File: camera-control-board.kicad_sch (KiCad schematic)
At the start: 24 parts, among them J1 DF12NB-36DS-0.5V_51_, J2 10104110-0001LF, J3 104031-0811, U1 STM32H743IITx, U2 IS42S32800J-7TLI, Y2 Crystal_GND2

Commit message: configured library and repo correctly. edits incoming
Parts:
- J1: symbol DF12NB-36DS-0.5V_51_:DF12NB-36DS-0.5V_51_ -> Argus_Connectors:DF12NB-36DS-0.5V_51_
- J2: symbol 10104110-0001LF:10104110-0001LF -> Argus_Connectors:10104110-0001LF
- J3: symbol 104031-0811:104031-0811 -> Argus_Connectors:104031-0811
- L1: symbol 2024-09-28_22-13-49:MPZ1608S181ATAH0 -> Argus_Misc:MPZ1608S181ATAH0
- RN1: symbol EXB-V8V103JV:EXB-V8V103JV -> Argus_Misc:EXB-V8V103JV
- U2: symbol IS42S32800J-7TLI:IS42S32800J-7TLI -> Argus_ICs:IS42S32800J-7TLI
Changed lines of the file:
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@@
 	)
 	(symbol
-		(lib_id "DF12NB-36DS-0.5V_51_:DF12NB-36DS-0.5V_51_")
+		(lib_id "Argus_Connectors:DF12NB-36DS-0.5V_51_")
 		(at 405.13 88.9 0)
 		(unit 1)
@@
 	)
 	(symbol
-		(lib_id "IS42S32800J-7TLI:IS42S32800J-7TLI")
+		(lib_id "Argus_ICs:IS42S32800J-7TLI")
 		(at 307.34 125.73 0)
 		(unit 1)
@@
 	)
 	(symbol
-		(lib_id "104031-0811:104031-0811")
+		(lib_id "Argus_Connectors:104031-0811")
 		(at 524.51 45.72 0)
 		(unit 1)
@@
 	)
 	(symbol
-		(lib_id "2024-09-28_22-13-49:MPZ1608S181ATAH0")
+		(lib_id "Argus_Misc:MPZ1608S181ATAH0")
 		(at 231.14 38.1 90)
 		(unit 1)
@@
 	)
 	(symbol
-		(lib_id "EXB-V8V103JV:EXB-V8V103JV")
+		(lib_id "Argus_Misc:EXB-V8V103JV")
 		(at 513.08 91.44 0)
 		(unit 1)
@@
 	)
 	(symbol
-		(lib_id "10104110-0001LF:10104110-0001LF")
+		(lib_id "Argus_Connectors:10104110-0001LF")
 		(at 107.95 322.58 0)
 		(unit 1)

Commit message: adding LDOs, changed schematic sheet size
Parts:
- added U3: XC6210B332MR-G, SOT-25_TOR, symbol Argus_ICs:XC6210B332MR-G
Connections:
- net VCC: no longer C1.1, C9.1, J1.2, J1.20, J1.30, J1.36, J3.4 (VDD), L1.1, R2.1, R3.1, R4.2, R7.1, RN1.1, RN1.2, RN1.3, RN1.4, U1.103 (VDD), U1.114 (VDD33_USB), U1.127 (VDD), U1.136 (VDD), U1.149 (VDD), U1.15 (VDD), U1.159 (VDD), U1.171 (PDR_ON), U1.172 (VDD), U1.23 (VDD), U1.36 (VDD), U1.49 (VDD), U1.6 (VBAT), U1.62 (VDD), U1.72 (VDD), U1.82 (VDD), U1.91 (VDD), U2.1 (VDD_2), U2.15 (VDD_3), U2.29 (VDD_4), U2.3 (VDDQ_2), U2.35 (VDDQ_5), U2.41 (VDDQ_8), U2.43 (VDD), U2.49 (VDDQ_3), U2.55 (VDDQ), U2.75 (VDDQ_4), U2.81 (VDDQ_6), U2.9 (VDDQ_7)
- new net +3.3V: C1.1, C9.1, J1.2, J1.20, J1.30, J1.36, J3.4 (VDD), L1.1, R2.1, R3.1, R4.2, R7.1, RN1.1, RN1.2, RN1.3, RN1.4, U1.103 (VDD), U1.114 (VDD33_USB), U1.127 (VDD), U1.136 (VDD), U1.149 (VDD), U1.15 (VDD), U1.159 (VDD), U1.171 (PDR_ON), U1.172 (VDD), U1.23 (VDD), U1.36 (VDD), U1.49 (VDD), U1.6 (VBAT), U1.62 (VDD), U1.72 (VDD), U1.82 (VDD), U1.91 (VDD), U2.1 (VDD_2), U2.15 (VDD_3), U2.29 (VDD_4), U2.3 (VDDQ_2), U2.35 (VDDQ_5), U2.41 (VDDQ_8), U2.43 (VDD), U2.49 (VDDQ_3), U2.55 (VDDQ), U2.75 (VDDQ_4), U2.81 (VDDQ_6), U2.9 (VDDQ_7)
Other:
- note added: "LDOs (Voltage Regulation)"
- note added: "MCU (STM32H743IITx)"
- moved on the sheet: C2, C3, C4, C5, C6, C7, C8, L1, R4, R5, R6, U1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

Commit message: Most of revisions finished. Added Flash.
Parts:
- removed C1: 47u, symbol Device:C_Polarized_US
- removed C2, C3: 12p, symbol Device:C
- removed C4: 1u, symbol Device:C
- removed C9: .1u, symbol Device:C
- removed R4: 10K, symbol Device:R
- removed RN1: EXB-V8V103JV, EXB38V472JV, symbol Argus_Misc:EXB-V8V103JV
- removed U3: XC6210B332MR-G, SOT-25_TOR, symbol Argus_ICs:XC6210B332MR-G
- removed Y2: Crystal_GND2, symbol Device:Crystal_GND2
- added C10, C19: 1uF, Capacitor_SMD:C_0603_1608Metric, symbol Device:C_Small
- added C11, C12: 4pF, Capacitor_SMD:C_0603_1608Metric, symbol Device:C_Small
- added C13, C14, C15, C16, C17, C3, C4: 0.1uF, Capacitor_SMD:C_0603_1608Metric, symbol Device:C_Small
- added C18: 47uF, Capacitor_SMD:C_0201_0603Metric, symbol Device:C_Polarized_Small_US
- added C2: 47uF, Capacitor_SMD:C_0603_1608Metric, symbol Device:C_Polarized_Small_US
- added D2: LED_RGBA, LED_SMD:LED_RGB_Wuerth-PLCC4_3.2x2.8mm_150141M173100, symbol Device:LED_RGBA
- added J4: 02x05 M 1.27mm, Connector_PinHeader_1.27mm:PinHeader_2x05_P1.27mm_Vertical_SMD, symbol Connector_Generic:Conn_02x05_Odd_Even
- added J5: Conn_01x08, Connector_PinHeader_2.54mm:PinHeader_1x08_P2.54mm_Vertical, symbol Connector_Generic:Conn_01x08
- added R10: 560, Resistor_SMD:R_0603_1608Metric, symbol Device:R
- added R11: 1K, Resistor_SMD:R_0603_1608Metric, symbol Device:R_Small
- added R16, R17, R18, R19, R20, R21, R8, R9: 10K, Resistor_SMD:R_0603_1608Metric, symbol Device:R_Small
- added R4: 100R, Resistor_SMD:R_0603_1608Metric, symbol Device:R_Small
- added RN2: 330R, Resistor_SMD:R_Array_Concave_4x0603, symbol Device:R_Pack04
- added SW1: CAS-120TA, cameraboard:CAS-120TA, symbol Switch:SW_SPDT
- added SW2: KMR2x, mainboard:BTN_KMR2, symbol Switch:SW_Push
- added U3: W25Q256JVEIQ TR, Argus_ICs:WSON8_E_WIN-L, symbol Argus_ICs:W25Q256JVEIQ_TR
- added U4: XC6210B332MR, Package_TO_SOT_SMD:SOT-23-5, symbol Regulator_Linear:XC6210B332MR
- added Y1: 12MHz/7pF, Crystal:Crystal_SMD_2520-4Pin_2.5x2.0mm, symbol Device:Crystal_GND24_Small
- C5, C6, C7, C8: footprint (none) -> Capacitor_SMD:C_0603_1608Metric
- J1: footprint DF12NB-36DS-0.5V_51_:HRS_DF12NB-36DS-0.5V_51_ -> Argus_Connectors:HRS_DF12NB-36DS-0.5V_51_
- J2: footprint 10104110-0001LF:AMPHENOL_10104110-0001LF -> Argus_Connectors:AMPHENOL_10104110-0001LF
- J3: footprint 104031-0811:MOLEX_104031-0811 -> Connector_Card:microSD_HC_Molex_104031-0811; symbol Argus_Connectors:104031-0811 -> Argus_Connectors:USD-1040310811
- R1, R2, R3, R5, R6: footprint (none) -> Resistor_SMD:R_0603_1608Metric
- R7: value R -> 10k
- U2: footprint IS42S32800J-7TLI:SOP50P1176X120-86N -> Argus_ICs:SOP50P1176X120-86N
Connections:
- net DRAM_CKE is gone; now on net DRAM_CLKE: U2.67 (CKE)
- net +3.3V: now also J1.10, C10.1, C13.2, C14.2, C15.2, C16.2, C17.2, C18.1, C19.2, C2.1, C3.2, D2.4 (A), J4.1 (Pin_1), J5.7 (Pin_7), R10.2, R11.1, R16.1, R17.1, R18.1, R19.1, R20.1, R21.1, R8.1, SW1.1 (A), U3.8 (VCC), U4.5 (VOUT)
- net BOOT0: now also R9.2
- net DRAM_D31: no longer U1.12 (PI10)
- net GND: now also J3.11 (SHD), C10.2, C11.1, C12.2, C13.1, C14.1, C15.1, C16.1, C17.1, C18.2, C19.1, C2.2, C3.1, C4.2, J4.3 (Pin_3), J4.5 (Pin_5), J5.8 (Pin_8), R4.2, RN2.4 (R4.1), RN2.5 (R4.2), SW1.3 (C), U3.4 (GND), U3.9 (EPAD), U4.2 (GND), Y1.2, Y1.4; no longer J3.10 (SW-2), J3.G1 (GND), J3.G2 (GND__1), J3.G3 (GND__2), J3.G4 (GND__3)
- net I2C1_SCL: now also J1.32, R2.2
- net I2C1_SDA: now also J1.34, R3.2
- net I2C2_SCL: now also J5.6 (Pin_6)
- net I2C2_SDA: now also J5.5 (Pin_5)
- net LED_B: now also RN2.3 (R3.1)
- net LED_G: now also RN2.2 (R2.1)
- net LED_R: now also RN2.1 (R1.1)
- net OSC_IN: now also C11.2, Y1.3
- net OSC_OUT: now also C12.1, Y1.1
- net SDIO_CMD: now also R17.2; no longer R7.2
- net SDIO_D0: now also J3.7 (DAT0), R18.2
- net SDIO_D1: now also J3.8 (DAT1), R19.2
- net SDIO_D2: now also J3.1 (DAT2), R20.2
- net SDIO_D3: now also J3.2 (DAT3/CD), R21.2
- net SD_CD: now also J3.10 (CD), R16.2
- net SPI2_MISO: now also J5.2 (Pin_2)
- net SPI2_MOSI: now also J5.1 (Pin_1)
- net SPI2_NSS: now also J5.4 (Pin_4)
- net SPI2_SCLK: now also J5.3 (Pin_3)
- net SWCLK: now also J4.4 (Pin_4), R11.2
- net SWDIO: now also J4.2 (Pin_2)
- net VBUS_R: now also R10.1
- net VCC: now also U4.1 (VIN), U4.3 (CE)
- net NRST: now reaches U1.31 (NRST)
- net NRST: now also C4.1, J4.10 (Pin_10), R8.2, SW2.2
- net FLASH_CS: now reaches U1.110 (PG6)
- net FLASH_CS: now also R7.2, U3.1 (/CS)
- net FLASH_IO3: now reaches U1.24 (PF6)
- net FLASH_IO3: now also U3.7 (/HOLD_OR_/RESET(IO3))
- net FLASH_IO2: now reaches U1.25 (PF7)
- net FLASH_IO2: now also U3.3 (/WP(IO2))
- net FLASH_IO0: now reaches U1.26 (PF8)
- net FLASH_IO0: now also U3.5 (DI(IO0))
- net FLASH_IO1: now reaches U1.27 (PF9)
- net FLASH_IO1: now also U3.2 (DO(IO1))
- net FLASH_CLK: now reaches U1.28 (PF10)
- net FLASH_CLK: now also U3.6 (CLK)
- new net: D2.1 (RK), RN2.8 (R1.2)
- new net: D2.2 (GK), RN2.7 (R2.2)
- new net: D2.3 (BK), RN2.6 (R3.2)
- new net: R4.1, SW2.1
- new net: R9.1, SW1.2 (B)
- no-connect marks 0 -> 4
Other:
- note added: "(Not Populated)"
- note added: "Decoupling Caps"
- note added: "Reset & Boot0 Switches"
- note added: "SWD Connector"
- note added: "Select boot mode Set "low" for normal operation. Set "high" for bootloader mode"
- note added: "Set for flight"
- note added: "Status LEDs, IO Headers"
- note added: "Status RGB LED"
- moved on the sheet: C5, C6, L1, R1, U2

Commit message: Schematic Revs Finished.
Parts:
- added C1: 1uF, Capacitor_SMD:C_0603_1608Metric, symbol Device:C_Small
- added VR1: AP7366-28W5-7, AP7366-28W5-7:SOT95P285X140-5N, symbol Argus_ICs:AP7366-28W5-7
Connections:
- net DCMI_FSIN: now also J4.6 (Pin_6)
- net GND: now also C1.2, VR1.2 (GND)
- net VCC: now also VR1.1 (IN), VR1.3 (EN)
- net VDDA: now also C1.1, VR1.5 (OUT)
- no-connect marks 4 -> 3
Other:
- note added: "Flash Memory"
- note added: "SD Card Connector"
- note removed: "(Not Populated)"
- moved on the sheet: C10, C11, C12, C13, C14, C15, C16, C17, C18, C19, C2, C3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

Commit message: all footprints accounted for.
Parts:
- removed SW2: KMR2x, mainboard:BTN_KMR2, symbol Switch:SW_Push
- added SW3: SW_Push, Argus_Misc:BTN_KMR2, symbol Switch:SW_Push
- L1: footprint IND_1608_TDK -> Argus_Misc:IND_1608_TDK
- R7: footprint (none) -> Resistor_SMD:R_0603_1608Metric
- SW1: footprint cameraboard:CAS-120TA -> Argus_Misc:CAS-120TA
- VR1: footprint AP7366-28W5-7:SOT95P285X140-5N -> Argus_ICs:SOT95P285X140-5N
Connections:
- net NRST: now also SW3.2
- net at R4.1: now also SW3.1
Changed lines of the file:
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@@
 	)
 	(symbol
-		(lib_id "Switch:SW_Push")
-		(at 179.07 72.39 0)
-		(unit 1)
-		(exclude_from_sim no)
-		(in_bom yes)
-		(on_board yes)
-		(dnp no)
-		(property "Reference" "SW2"
-			(at 179.07 65.786 0)
-			(effects
-				(font
-					(size 1.27 1.27)
-				)
-			)
-		)
-		(property "Value" "KMR2x"
-			(at 179.07 68.0974 0)
-			(effects
-				(font
-					(size 1.27 1.27)
-				)
-			)
-		)
-		(property "Footprint" "mainboard:BTN_KMR2"
-			(at 179.07 67.31 0)
-			(effects
-				(font
-					(size 1.27 1.27)
-				)
-				(hide yes)
-			)
-		)
-		(property "Datasheet" "~"
-			(at 179.07 67.31 0)
-			(effects
-				(font
-					(size 1.27 1.27)
-				)
-				(hide yes)
-			)
-		)
-		(property "Description" ""
-			(at 179.07 72.39 0)
-			(effects
-				(font
-					(size 1.27 1.27)
-				)
-				(hide yes)
-			)
-		)
-		(pin "1"
-		)
-		(pin "2"
-		)
-		(instances
-			(project "camera-control-board"
-				(path "/a6ed6f18-4f86-494f-813d-c58250854c51"
-					(reference "SW2")
-					(unit 1)
-				)
-			)
-		)
-	)
-	(symbol
 		(lib_id "power:VCC")
 		(at 156.21 27.94 0)
@@
 			)
 		)
-		(property "Footprint" "cameraboard:CAS-120TA"
+		(property "Footprint" "Argus_Misc:CAS-120TA"
 			(at 217.932 71.12 0)
 			(effects
@@
 			)
 		)
-		(property "Footprint" ""
+		(property "Footprint" "Resistor_SMD:R_0603_1608Metric"
 			(at 278.892 204.47 90)
 			(effects
@@
 			)
 		)
-		(property "Footprint" "IND_1608_TDK"
+		(property "Footprint" "Argus_Misc:IND_1608_TDK"
 			(at 123.19 34.29 0)
 			(effects
@@
 	)
 	(symbol
+		(lib_id "Switch:SW_Push")
+		(at 179.07 72.39 0)
+		(unit 1)
+		(exclude_from_sim no)
+		(in_bom yes)
+		(on_board yes)
+		(dnp no)
+		(fields_autoplaced yes)
+		(property "Reference" "SW3"
+			(at 179.07 64.77 0)
+			(effects
+				(font
+					(size 1.27 1.27)
+				)
+			)
+		)
+		(property "Value" "SW_Push"
+			(at 179.07 67.31 0)
+			(effects
+				(font
+					(size 1.27 1.27)
+				)
+			)
+		)
+		(property "Footprint" "Argus_Misc:BTN_KMR2"
+			(at 179.07 67.31 0)
+			(effects
+				(font
+					(size 1.27 1.27)
+				)
+				(hide yes)
+			)
+		)
+		(property "Datasheet" "~"
+			(at 179.07 67.31 0)
+			(effects
+				(font
+					(size 1.27 1.27)
+				)
+				(hide yes)
+			)
+		)
+		(property "Description" "Push button switch, generic, two pins"
+			(at 179.07 72.39 0)
+			(effects
+				(font
+					(size 1.27 1.27)
+				)
+				(hide yes)
+			)
+		)
+		(pin "1"
+		)
+		(pin "2"
+		)
+		(instances
+			(project ""
+				(path "/a6ed6f18-4f86-494f-813d-c58250854c51"
+					(reference "SW3")
+					(unit 1)
+				)
+			)
+		)
+	)
+	(symbol
 		(lib_id "power:GND")
 		(at 252.73 36.957 0)
@@
 			)
 		)
-		(property "Footprint" "AP7366-28W5-7:SOT95P285X140-5N"
+		(property "Footprint" "Argus_ICs:SOT95P285X140-5N"
 			(at 233.68 31.75 0)
 			(effects

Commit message: Layout begun.
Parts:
- J5: value Conn_01x08 -> Conn_01x09; footprint Connector_PinHeader_2.54mm:PinHeader_1x08_P2.54mm_Vertical -> Connector_PinHeader_2.54mm:PinHeader_1x09_P2.54mm_Vertical; symbol Connector_Generic:Conn_01x08 -> Connector_Generic:Conn_01x09
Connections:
- net +3.3V: now also J5.8 (Pin_8); no longer J5.7 (Pin_7)
- net DCMI_FSIN: now also J5.1 (Pin_1); no longer J4.6 (Pin_6)
- net GND: now also J5.9 (Pin_9); no longer J5.8 (Pin_8)
- net I2C2_SCL: now also J5.7 (Pin_7); no longer J5.6 (Pin_6)
- net I2C2_SDA: now also J5.6 (Pin_6); no longer J5.5 (Pin_5)
- net SPI2_MISO: now also J5.3 (Pin_3); no longer J5.2 (Pin_2)
- net SPI2_MOSI: now also J5.2 (Pin_2); no longer J5.1 (Pin_1)
- net SPI2_NSS: now also J5.5 (Pin_5); no longer J5.4 (Pin_4)
- net SPI2_SCLK: now also J5.4 (Pin_4); no longer J5.3 (Pin_3)
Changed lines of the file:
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@@
 	(wire
 		(pts
+			(xy 198.12 100.33) (xy 209.55 100.33)
+		)
+		(stroke
+			(width 0)
+			(type default)
+		)
+	)
+	(wire
+		(pts
 			(xy 352.806 106.68) (xy 352.806 111.76)
 		)
@@
 	(wire
 		(pts
-			(xy 176.276 113.157) (xy 187.706 113.157)
-		)
-		(stroke
-			(width 0)
-			(type default)
-		)
-	)
-	(wire
-		(pts
 			(xy 34.29 73.66) (xy 46.99 73.66)
 		)
@@
 		)
 	)
+	(label "DCMI_FSIN"
+		(at 199.39 100.33 0)
+		(fields_autoplaced yes)
+		(effects
+			(font
+				(size 1.27 1.27)
+			)
+			(justify left bottom)
+		)
+	)
 	(label "I2C2_SDA"
 		(at 197.866 113.03 0)
@@
 		)
 	)
-	(label "DCMI_FSIN"
-		(at 177.546 113.157 0)
-		(fields_autoplaced yes)
-		(effects
-			(font
-				(size 1.27 1.27)
-			)
-			(justify left bottom)
-		)
-	)
 	(label "DRAM_D19"
 		(at 38.1 132.08 0)
@@
 	)
 	(symbol
-		(lib_id "Connector_Generic:Conn_01x08")
+		(lib_id "Connector_Generic:Conn_01x09")
 		(at 214.63 110.49 0)
 		(unit 1)
 		(exclude_from_sim no)
 		(in_bom yes)
-		(on_board no)
+		(on_board yes)
 		(dnp no)
 		(property "Reference" "J5"
@@
 			)
 		)
-		(property "Value" "Conn_01x08"
+		(property "Value" "Conn_01x09"
 			(at 208.788 99.441 0)
 			(effects
@@
 			)
 		)
-		(property "Footprint" "Connector_PinHeader_2.54mm:PinHeader_1x08_P2.54mm_Vertical"
+		(property "Footprint" "Connector_PinHeader_2.54mm:PinHeader_1x09_P2.54mm_Vertical"
 			(at 214.63 110.49 0)
 			(effects
@@
 			)
 		)
-		(property "Description" ""
+		(property "Description" "Generic connector, single row, 01x09, script generated (kicad-library-utils/schlib/autogen/connector/)"
 			(at 214.63 110.49 0)
 			(effects
@@
 		(pin "8"
 		)
+		(pin "9"
+		)
 		(instances

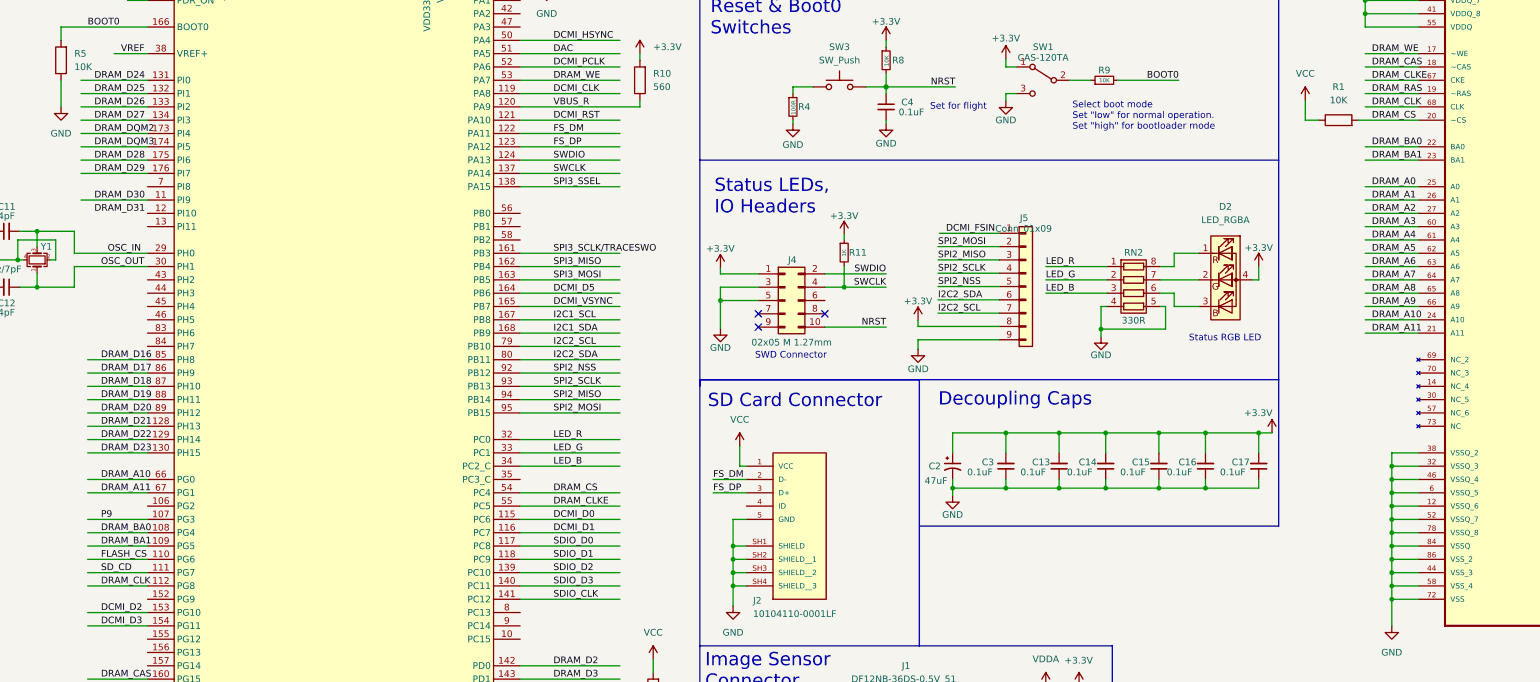
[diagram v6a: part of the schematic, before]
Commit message: layout 45deg
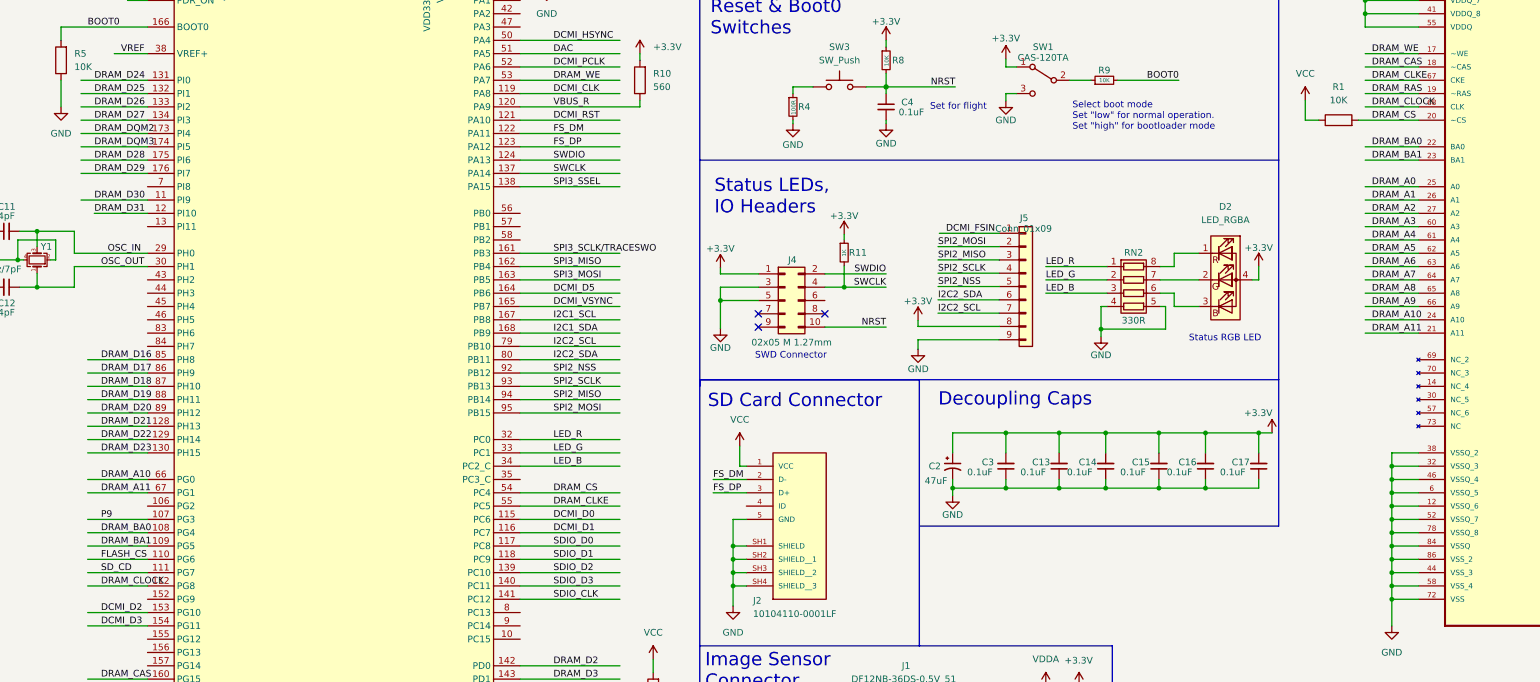
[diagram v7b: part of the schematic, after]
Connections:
- net DRAM_D31: now also U1.12 (PI10)
- net DRAM_CLK renamed DRAM_CLOCK
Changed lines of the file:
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@@
 	(wire
 		(pts
+			(xy 36.83 96.52) (xy 46.99 96.52)
+		)
+		(stroke
+			(width 0)
+			(type default)
+		)
+	)
+	(wire
+		(pts
 			(xy 220.98 138.43) (xy 220.98 142.24)
 		)
@@
 		)
 	)
-	(label "DRAM_CLK"
-		(at 280.67 76.2 0)
-		(fields_autoplaced yes)
-		(effects
-			(font
-				(size 1.27 1.27)
-			)
-			(justify left bottom)
-		)
-	)
 	(label "DRAM_D12"
 		(at 124.46 264.16 0)
@@
 		)
 	)
-	(label "DRAM_CLK"
+	(label "DRAM_CLOCK"
 		(at 38.1 167.64 0)
 		(fields_autoplaced yes)
@@
 		(fields_autoplaced yes)
 		(effects
+			(font
+				(size 1.27 1.27)
+			)
+			(justify left bottom)
+		)
+	)
+	(label "DRAM_CLOCK"
+		(at 280.67 76.2 0)
+		(fields_autoplaced yes)
+		(effects

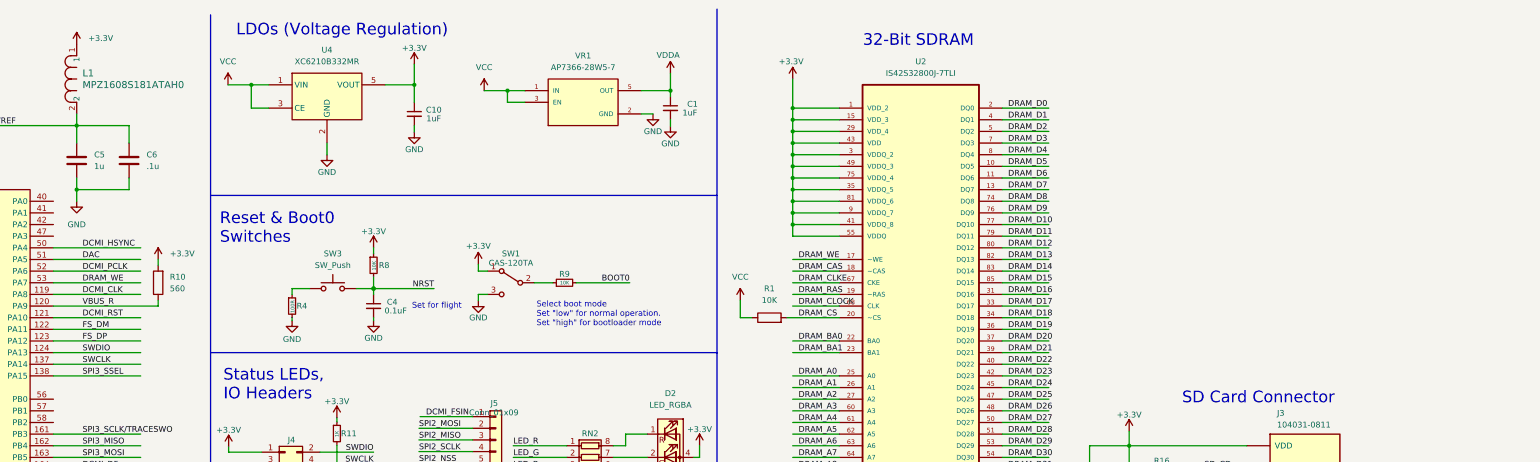
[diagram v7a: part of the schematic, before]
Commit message: Updated to add USB-C Connection.
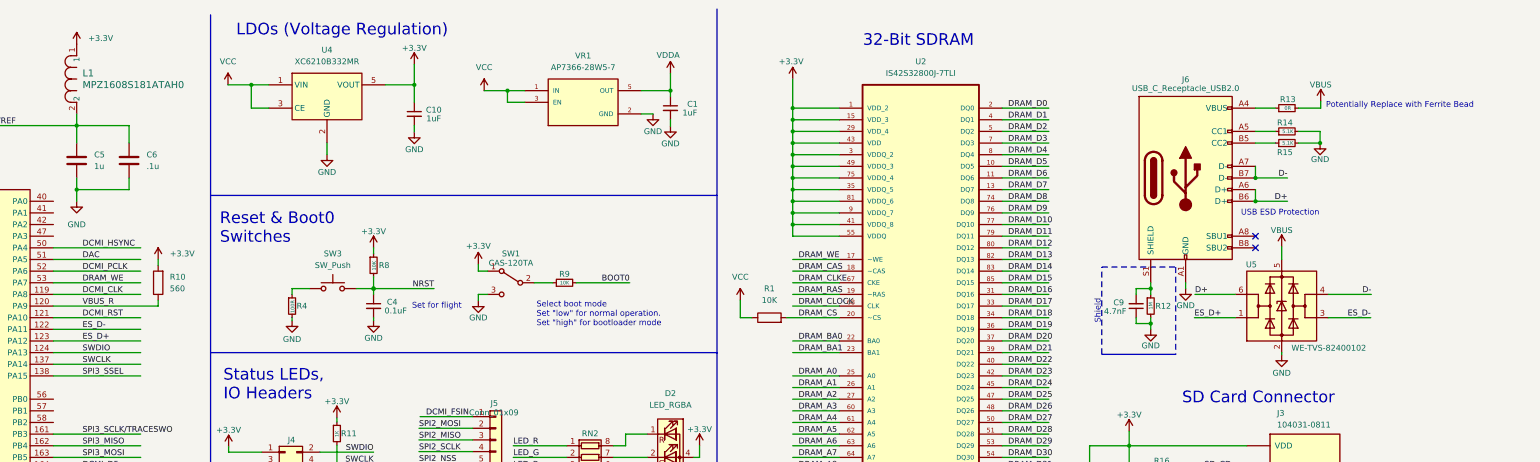
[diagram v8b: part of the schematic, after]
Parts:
- added C9: 4.7nF, Capacitor_SMD:C_0603_1608Metric, symbol Device:C_Small
- added J6: USB_C_Receptacle_USB2.0, Connector_USB:USB_C_Receptacle_HRO_TYPE-C-31-M-12, symbol Connector:USB_C_Receptacle_USB2.0
- added R12: 1M, Resistor_SMD:R_0603_1608Metric, symbol Device:R_Small
- added R13: 0R, Resistor_SMD:R_0603_1608Metric, symbol Device:R_Small
- added R14, R15: 5.1K, Resistor_SMD:R_0603_1608Metric, symbol Device:R_Small
- added U5: WE-TVS-82400102, Package_TO_SOT_SMD:SOT-23-6, symbol Power_Protection:USBLC6-2SC6
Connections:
- net FS_DM: no longer U1.122 (PA11)
- net FS_DP: no longer U1.123 (PA12)
- net GND: now also C9.1, J6.A1 (GND), J6.A12 (GND), J6.B1 (GND), J6.B12 (GND), R12.2, R14.2, R15.2, U5.2 (GND)
- new net: C9.2, J6.S1 (SHIELD), R12.1
- new net: J6.A5 (CC1), R14.1
- new net: J6.B5 (CC2), R15.1
- new net: J6.A4 (VBUS), J6.A9 (VBUS), J6.B4 (VBUS), J6.B9 (VBUS), R13.1
- new net D+: J6.A6 (D+), J6.B6 (D+), U5.6 (I/O1)
- new net D-: J6.A7 (D-), J6.B7 (D-), U5.4 (I/O2)
- new net ES_D+: U1.123 (PA12), U5.1 (I/O1)
- new net ES_D-: U1.122 (PA11), U5.3 (I/O2)
- new net VBUS: R13.2, U5.5 (VBUS)
- no-connect marks 3 -> 5
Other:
- note added: "Potentially Replace with Ferrite Bead"
- note added: "Shield"
- note added: "USB ESD Protection"
